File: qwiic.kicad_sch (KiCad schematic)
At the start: 1 part, among them J2 PinHeader_2x10_P1.27mm_SMD_Sh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

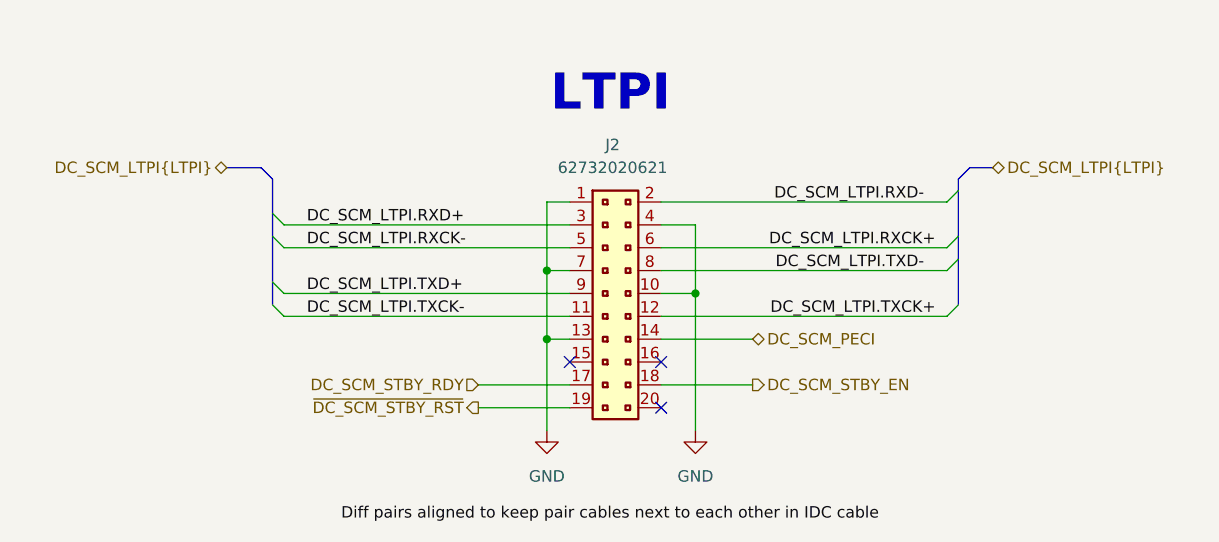
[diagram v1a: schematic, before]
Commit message: [#92504] Connect QWIIC connector
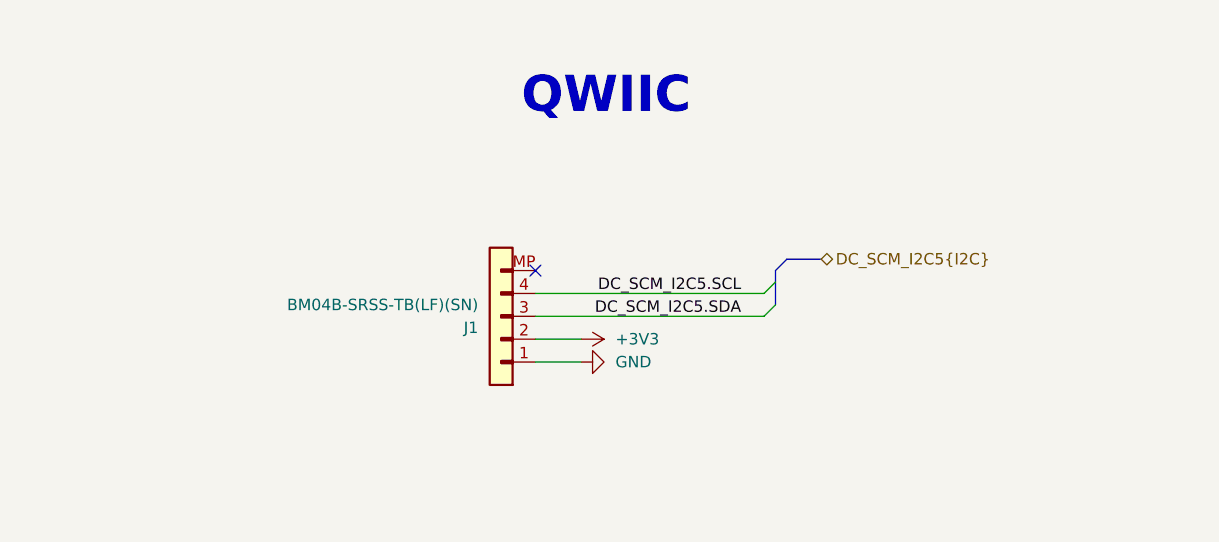
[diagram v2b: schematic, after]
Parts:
- removed J2: PinHeader_2x10_P1.27mm_SMD_Shrouded, antmicro-footprints:PinHeader_2x10_P1.27mm_SMD_Shrouded, symbol antmicroGenericPinHeaders:PinHeader_2x10_P1.27mm_SMD_Shrouded
- added J1: JST_SH_1x4_BM04B-SRSS-TB-LF-SN, antmicro-footprints:Conn_JST_SH_1x4_BM04B-SRSS-TB-LF-SN, symbol antmicroWire2BoardConnectors:JST_SH_1x4_BM04B-SRSS-TB-LF-SN
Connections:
- net GND: now also J1.1
- new net +3V3: J1.2
- new net DC_SCM_I2C5.SCL: J1.4
- new net DC_SCM_I2C5.SDA: J1.3
- no-connect marks 3 -> 1
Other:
- note added: "QWIIC"
- note removed: "LTPI"

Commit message: [#92504] Add pull-up resistors for QWIIC
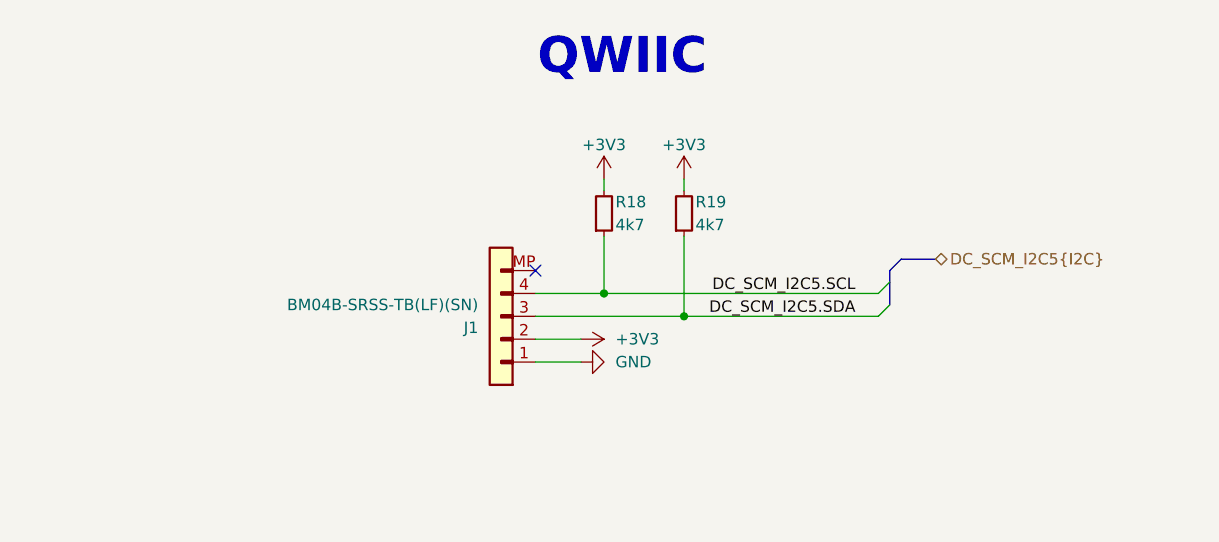
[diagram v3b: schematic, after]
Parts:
- added R18, R19: R_4k7_0402, antmicro-footprints:R_0402_1005Metric, symbol antmicroResistors0402:R_4k7_0402
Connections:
- net +3V3: now also R18.2, R19.2
- net DC_SCM_I2C5.SCL: now also R18.1
- net DC_SCM_I2C5.SDA: now also R19.1

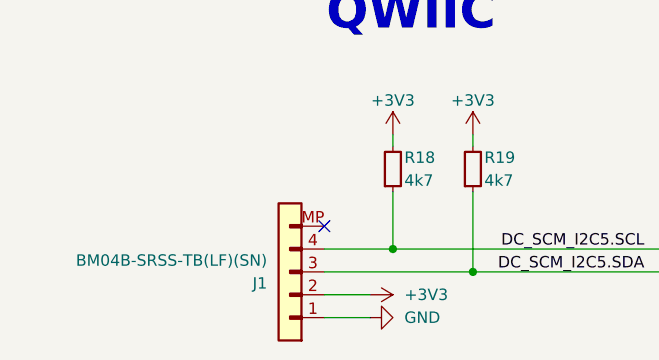
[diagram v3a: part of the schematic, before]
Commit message: [#92504] Update Annotation for connectors
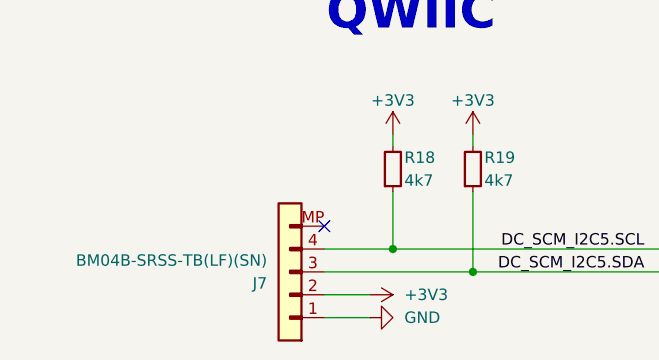
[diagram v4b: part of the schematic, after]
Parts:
- renumbered J1 to J7
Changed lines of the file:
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@@
 		(on_board yes)
 		(dnp no)
-		(property "Reference" "J1"
+		(property "Reference" "J7"
 			(at 59.69 50.8 0)
 			(effects
@@
 			(project ""
 				(path "/5d67ef28-5805-4f87-b722-2926dabf7f6e/d9b5a36f-f960-4ce7-8269-f56a658e52fc"
-					(reference "J1")
+					(reference "J7")
 					(unit 1)
 				)
